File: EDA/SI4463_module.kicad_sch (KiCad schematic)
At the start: 43 parts, among them J1 EXT_ANT, J2 Conn_01x10_Pin, J3 U. FL, U1 SI4463-C2A-GMR, U2 SKY66423-11, Y1 30MHz

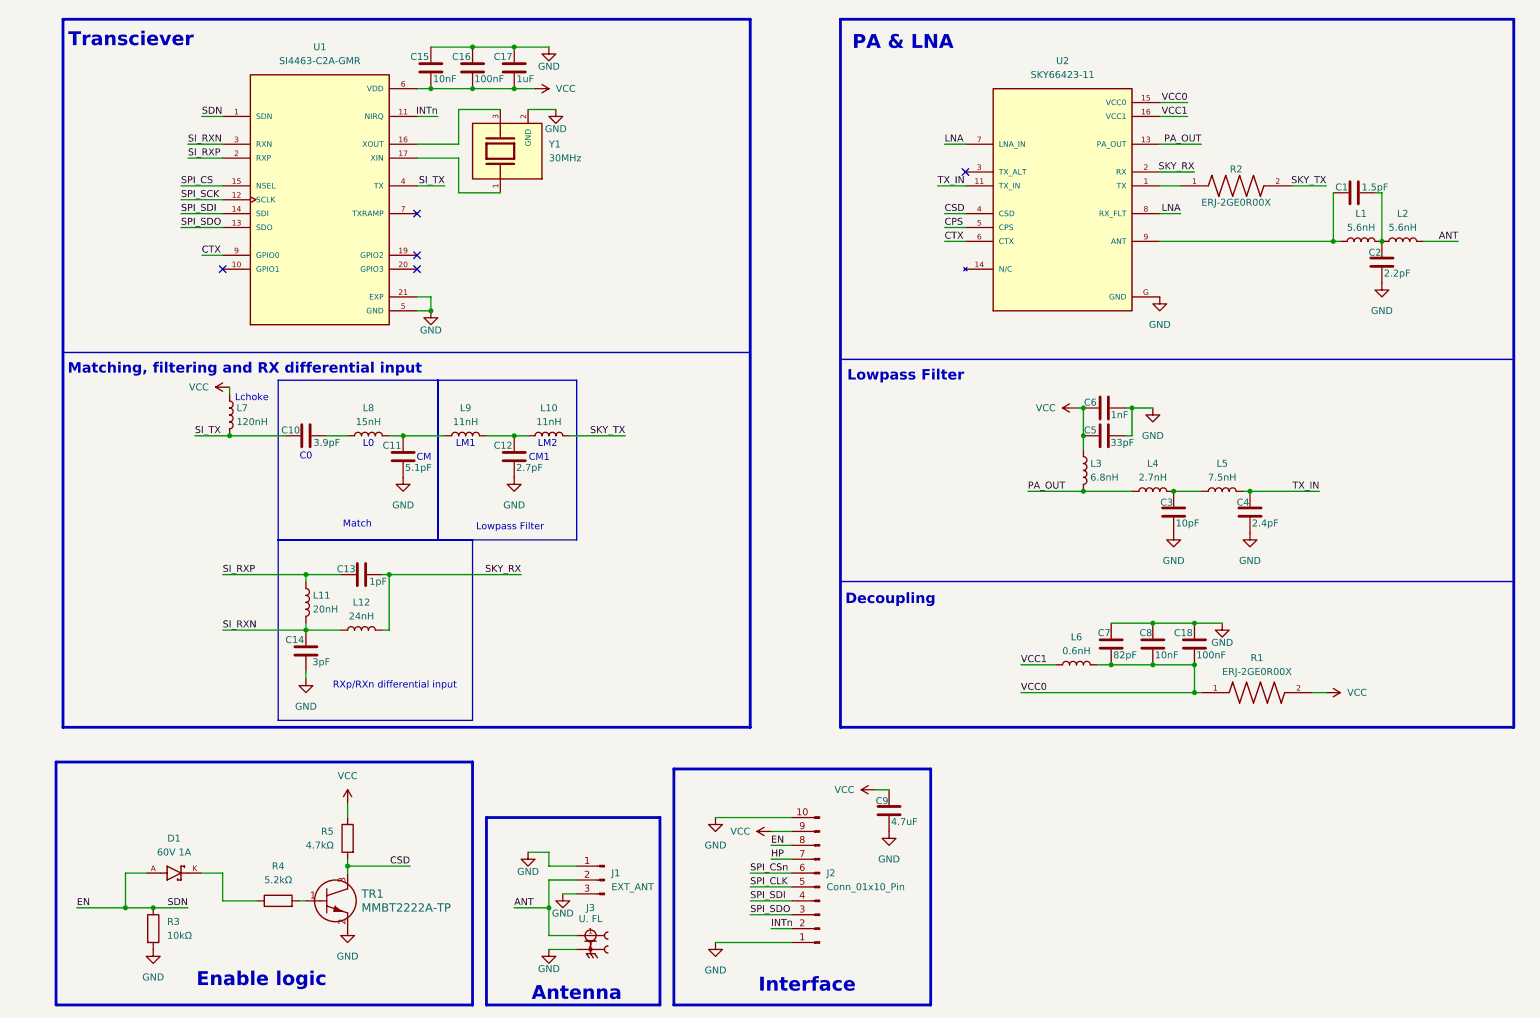
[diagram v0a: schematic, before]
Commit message: Added edge headers, and assigned MPN's and footprints.
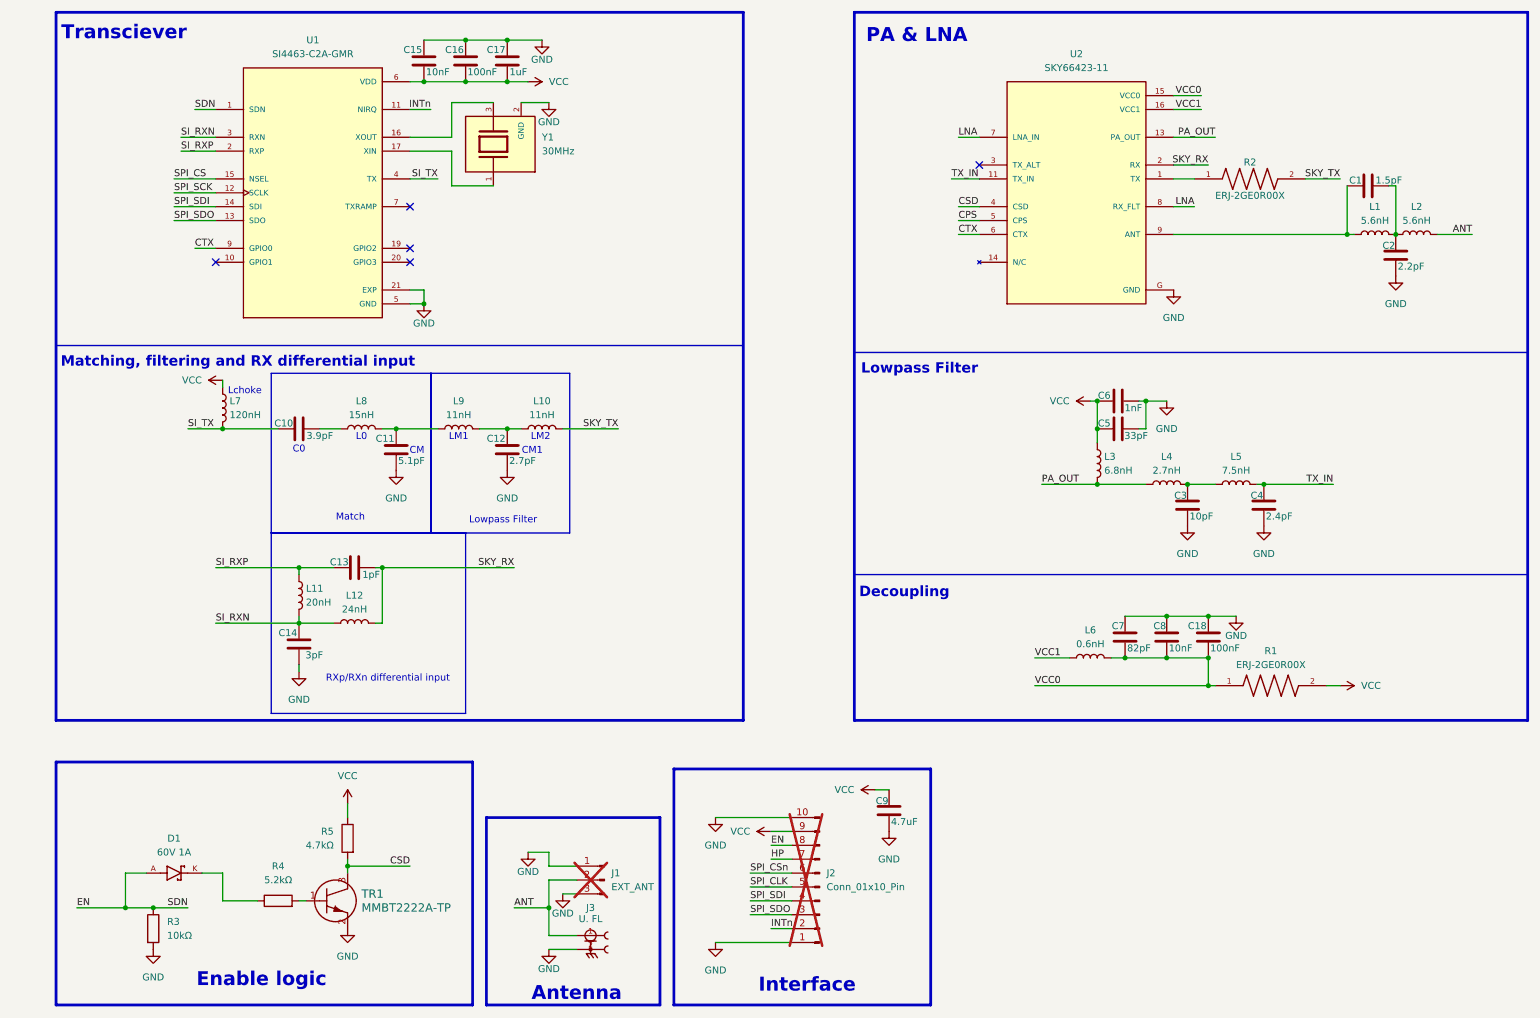
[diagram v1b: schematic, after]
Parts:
- C1: footprint (none) -> Capacitor_SMD:C_0402_1005Metric; MP (none) -> QSCF500Q1R5B1GV001T
- C10: footprint (none) -> Capacitor_SMD:C_0402_1005Metric; MP (none) -> QSCF500Q3R9C1GV001T
- C11: footprint (none) -> Capacitor_SMD:C_0402_1005Metric; MP (none) -> QSCF500Q5R1C1GV001T
- C12: footprint (none) -> Capacitor_SMD:C_0402_1005Metric; MP (none) -> QSCF500Q2R7B1GV001T
- C13: footprint (none) -> Capacitor_SMD:C_0402_1005Metric; MP (none) -> QSCF500Q1R0B1GV001T
- C14: footprint (none) -> Capacitor_SMD:C_0402_1005Metric; MP (none) -> QSCF500Q3R0B1GV001T
- C15, C8: footprint (none) -> Capacitor_SMD:C_0603_1608Metric; MP (none) -> C0603C103F3GECAUTO
- C16, C18: footprint (none) -> Capacitor_SMD:C_1206_3216Metric; MP (none) -> C1206C104F3GECTU
- C17: footprint (none) -> Capacitor_SMD:C_0603_1608Metric; MP (none) -> NMC0603X7R105K16TRPF
- C2: footprint (none) -> Capacitor_SMD:C_0402_1005Metric; MP (none) -> QSCF251Q2R2A1GV001T
- C3: footprint (none) -> Capacitor_SMD:C_0402_1005Metric; MP (none) -> QSCF500Q100J1GV001T
- C4: footprint (none) -> Capacitor_SMD:C_0402_1005Metric; MP (none) -> QSCF500Q2R4B1GV001T
- C5: footprint (none) -> Capacitor_SMD:C_0402_1005Metric; MP (none) -> QSCF500Q330F1GV001T
- C6: footprint (none) -> Capacitor_SMD:C_0402_1005Metric; MP (none) -> C0402C102F5GECAUTO
- C7: footprint (none) -> Capacitor_SMD:C_0402_1005Metric; MP (none) -> CBR04C820F3GAC
- C9: footprint (none) -> Capacitor_SMD:C_0603_1608Metric; MP (none) -> NMC0603X5R475K6.3TRPF
- J1: footprint (none) -> module-lib:PinHeader_1x03_P2.00mm_Vertical; now not fitted; now left out of the parts list
- J2: footprint (none) -> module-lib:PinHeader_1x10_P2.00mm_Vertical; now not fitted; now left out of the parts list
- L1, L2: footprint (none) -> Inductor_SMD:L_0402_1005Metric; MP (none) -> WCI1005CP5N6GDG
- L10, L9: footprint (none) -> Inductor_SMD:L_0201_0603Metric; MP (none) -> BWCM0006040411NJ00
- L11: footprint (none) -> Inductor_SMD:L_0402_1005Metric; MP (none) -> WCI1005CP20NGDG
- L12: footprint (none) -> Inductor_SMD:L_0805_2012Metric; MP (none) -> LQW2BAS24NJ00L
- L3: footprint (none) -> Inductor_SMD:L_0402_1005Metric; MP (none) -> WCI1005CP6N8GDG
- L4: footprint (none) -> Inductor_SMD:L_0402_1005Metric; MP (none) -> AISC-Q0402HQ-2N7C-T
- L5: footprint (none) -> Inductor_SMD:L_0402_1005Metric; MP (none) -> WCI1005CP7N5GDG
- L6: footprint (none) -> Inductor_SMD:L_0201_0603Metric; MP (none) -> LQP03TN0N6B02D
- L7: footprint (none) -> Inductor_SMD:L_0603_1608Metric; MP (none) -> 744917212
- L8: footprint (none) -> Inductor_SMD:L_0402_1005Metric; MP (none) -> LRW0402WG15NGG001T
- R3: footprint (none) -> Resistor_SMD:R_0402_1005Metric; MP (none) -> RC0402FR-0710KL
- R4: footprint (none) -> Resistor_SMD:R_0805_2012Metric; MP (none) -> RT0805BRD075K2L
- R5: footprint (none) -> Resistor_SMD:R_0402_1005Metric; MP (none) -> RC0402JR-074K7L
- TR1: MP (none) -> MMBT2222A-TP
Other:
- moved on the sheet: C1, C10, C11, C12, C13, C14, C15, C16, C17, C18, C2, C3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

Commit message: Made PCB, placed components, routed almost all of them (missing power traces). added EMI shield.
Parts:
- added H1: WE-SHC_SEAMLESS, module-lib:WE-SHC_SEAMLESS_3670310, symbol module:WE-SHC_SEAMLESS
- added R6: 10kΩ, Resistor_SMD:R_0402_1005Metric, symbol Device:R
- R1, R2: value ERJ-2GE0R00X -> 0Ω
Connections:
- net HP is gone; now on net CPS: J2.7 (Pin_7)
- net SPI_CS is gone; now on net SPI_CSn: U1.15 (NSEL)
- net SPI_SCK is gone; now on net SPI_CLK: U1.12 (SCLK)
- net CPS: now also R6.1
- net GND: now also H1.1, H1.2, H1.3, H1.4, R6.2
- net SPI_CLK: now also J2.3 (Pin_3); no longer J2.5 (Pin_5)
- net SPI_SDI: now also J2.5 (Pin_5); no longer J2.4 (Pin_4)
- net SPI_SDO: now also J2.4 (Pin_4); no longer J2.3 (Pin_3)
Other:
- moved on the sheet: C9
